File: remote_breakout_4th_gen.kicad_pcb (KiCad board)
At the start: 2 copper layers, 12.5 x 12.1 mm, 3 parts, among them J1 Conn_01x04, J2 Conn_02x04_Odd_Even, J3 Conn_01x04

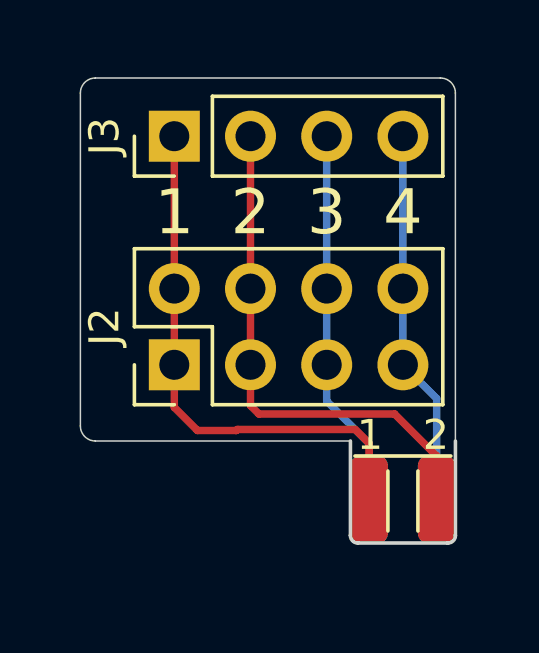
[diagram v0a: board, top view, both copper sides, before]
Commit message: Fill unused areas with copper, update remote connector with connector pads
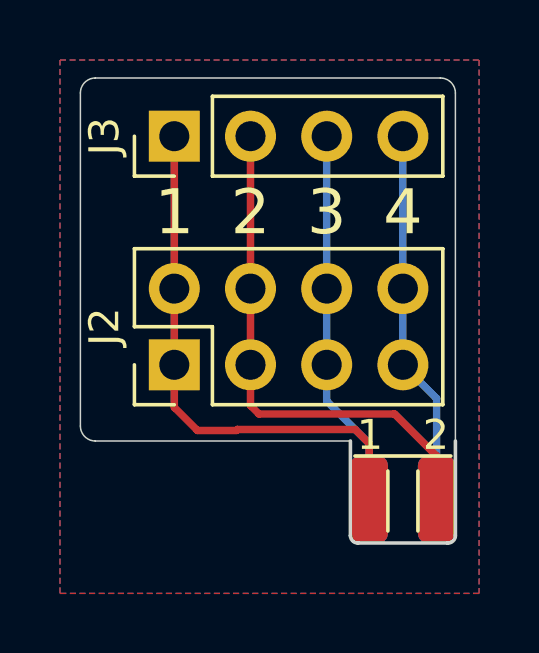
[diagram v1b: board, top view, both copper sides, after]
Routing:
- added copper zone on B.Cu, net (none)
- added copper zone on F.Cu, net (none)
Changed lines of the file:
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@@
       (effects (font (size 1 1) (thickness 0.15)))
     )
+    (fp_text user %R (at 0 3.81) (layer F.Fab)
+      (effects (font (size 1 1) (thickness 0.15)))
+    )
+    (fp_line (start -0.635 -1.27) (end 1.27 -1.27) (layer F.Fab) (width 0.1))
+    (fp_line (start 1.27 -1.27) (end 1.27 8.89) (layer F.Fab) (width 0.1))
+    (fp_line (start 1.27 8.89) (end -1.27 8.89) (layer F.Fab) (width 0.1))
+    (fp_line (start -1.27 8.89) (end -1.27 -0.635) (layer F.Fab) (width 0.1))
+    (fp_line (start -1.27 -0.635) (end -0.635 -1.27) (layer F.Fab) (width 0.1))
+    (fp_line (start -1.33 8.95) (end 1.33 8.95) (layer F.SilkS) (width 0.12))
+    (fp_line (start -1.33 1.27) (end -1.33 8.95) (layer F.SilkS) (width 0.12))
+    (fp_line (start 1.33 1.27) (end 1.33 8.95) (layer F.SilkS) (width 0.12))
+    (fp_line (start -1.33 1.27) (end 1.33 1.27) (layer F.SilkS) (width 0.12))
+    (fp_line (start -1.33 0) (end -1.33 -1.33) (layer F.SilkS) (width 0.12))
+    (fp_line (start -1.33 -1.33) (end 0 -1.33) (layer F.SilkS) (width 0.12))
+    (fp_line (start -1.8 -1.8) (end -1.8 9.4) (layer F.CrtYd) (width 0.05))
+    (fp_line (start -1.8 9.4) (end 1.8 9.4) (layer F.CrtYd) (width 0.05))
+    (fp_line (start 1.8 9.4) (end 1.8 -1.8) (layer F.CrtYd) (width 0.05))
     (fp_line (start 1.8 -1.8) (end -1.8 -1.8) (layer F.CrtYd) (width 0.05))
-    (fp_line (start 1.8 9.4) (end 1.8 -1.8) (layer F.CrtYd) (width 0.05))
-    (fp_line (start -1.8 9.4) (end 1.8 9.4) (layer F.CrtYd) (width 0.05))
-    (fp_line (start -1.8 -1.8) (end -1.8 9.4) (layer F.CrtYd) (width 0.05))
-    (fp_line (start -1.33 -1.33) (end 0 -1.33) (layer F.SilkS) (width 0.12))
-    (fp_line (start -1.33 0) (end -1.33 -1.33) (layer F.SilkS) (width 0.12))
-    (fp_line (start -1.33 1.27) (end 1.33 1.27) (layer F.SilkS) (width 0.12))
-    (fp_line (start 1.33 1.27) (end 1.33 8.95) (layer F.SilkS) (width 0.12))
-    (fp_line (start -1.33 1.27) (end -1.33 8.95) (layer F.SilkS) (width 0.12))
-    (fp_line (start -1.33 8.95) (end 1.33 8.95) (layer F.SilkS) (width 0.12))
-    (fp_line (start -1.27 -0.635) (end -0.635 -1.27) (layer F.Fab) (width 0.1))
-    (fp_line (start -1.27 8.89) (end -1.27 -0.635) (layer F.Fab) (width 0.1))
-    (fp_line (start 1.27 8.89) (end -1.27 8.89) (layer F.Fab) (width 0.1))
-    (fp_line (start 1.27 -1.27) (end 1.27 8.89) (layer F.Fab) (width 0.1))
-    (fp_line (start -0.635 -1.27) (end 1.27 -1.27) (layer F.Fab) (width 0.1))
-    (fp_text user %R (at 0 3.81) (layer F.Fab)
-      (effects (font (size 1 1) (thickness 0.15)))
-    )
     (pad 4 thru_hole oval (at 0 7.62 90) (size 1.7 1.7) (drill 1) (layers *.Cu *.Mask)
       (net 3 /4))
@@
       (effects (font (size 1 1) (thickness 0.15)))
     )
+    (fp_text user %R (at 1.27 3.81) (layer F.Fab)
+      (effects (font (size 1 1) (thickness 0.15)))
+    )
+    (fp_line (start 0 -1.27) (end 3.81 -1.27) (layer F.Fab) (width 0.1))
+    (fp_line (start 3.81 -1.27) (end 3.81 8.89) (layer F.Fab) (width 0.1))
+    (fp_line (start 3.81 8.89) (end -1.27 8.89) (layer F.Fab) (width 0.1))
+    (fp_line (start -1.27 8.89) (end -1.27 0) (layer F.Fab) (width 0.1))
+    (fp_line (start -1.27 0) (end 0 -1.27) (layer F.Fab) (width 0.1))
+    (fp_line (start -1.33 8.95) (end 3.87 8.95) (layer F.SilkS) (width 0.12))
+    (fp_line (start -1.33 1.27) (end -1.33 8.95) (layer F.SilkS) (width 0.12))
+    (fp_line (start 3.87 -1.33) (end 3.87 8.95) (layer F.SilkS) (width 0.12))
+    (fp_line (start -1.33 1.27) (end 1.27 1.27) (layer F.SilkS) (width 0.12))
+    (fp_line (start 1.27 1.27) (end 1.27 -1.33) (layer F.SilkS) (width 0.12))
+    (fp_line (start 1.27 -1.33) (end 3.87 -1.33) (layer F.SilkS) (width 0.12))
+    (fp_line (start -1.33 0) (end -1.33 -1.33) (layer F.SilkS) (width 0.12))
+    (fp_line (start -1.33 -1.33) (end 0 -1.33) (layer F.SilkS) (width 0.12))
+    (fp_line (start -1.8 -1.8) (end -1.8 9.4) (layer F.CrtYd) (width 0.05))
+    (fp_line (start -1.8 9.4) (end 4.35 9.4) (layer F.CrtYd) (width 0.05))
+    (fp_line (start 4.35 9.4) (end 4.35 -1.8) (layer F.CrtYd) (width 0.05))
     (fp_line (start 4.35 -1.8) (end -1.8 -1.8) (layer F.CrtYd) (width 0.05))
-    (fp_line (start 4.35 9.4) (end 4.35 -1.8) (layer F.CrtYd) (width 0.05))
-    (fp_line (start -1.8 9.4) (end 4.35 9.4) (layer F.CrtYd) (width 0.05))
-    (fp_line (start -1.8 -1.8) (end -1.8 9.4) (layer F.CrtYd) (width 0.05))
-    (fp_line (start -1.33 -1.33) (end 0 -1.33) (layer F.SilkS) (width 0.12))
-    (fp_line (start -1.33 0) (end -1.33 -1.33) (layer F.SilkS) (width 0.12))
-    (fp_line (start 1.27 -1.33) (end 3.87 -1.33) (layer F.SilkS) (width 0.12))
-    (fp_line (start 1.27 1.27) (end 1.27 -1.33) (layer F.SilkS) (width 0.12))
-    (fp_line (start -1.33 1.27) (end 1.27 1.27) (layer F.SilkS) (width 0.12))
-    (fp_line (start 3.87 -1.33) (end 3.87 8.95) (layer F.SilkS) (width 0.12))
-    (fp_line (start -1.33 1.27) (end -1.33 8.95) (layer F.SilkS) (width 0.12))
-    (fp_line (start -1.33 8.95) (end 3.87 8.95) (layer F.SilkS) (width 0.12))
-    (fp_line (start -1.27 0) (end 0 -1.27) (layer F.Fab) (width 0.1))
-    (fp_line (start -1.27 8.89) (end -1.27 0) (layer F.Fab) (width 0.1))
-    (fp_line (start 3.81 8.89) (end -1.27 8.89) (layer F.Fab) (width 0.1))
-    (fp_line (start 3.81 -1.27) (end 3.81 8.89) (layer F.Fab) (width 0.1))
-    (fp_line (start 0 -1.27) (end 3.81 -1.27) (layer F.Fab) (width 0.1))
-    (fp_text user %R (at 1.27 3.81) (layer F.Fab)
-      (effects (font (size 1 1) (thickness 0.15)))
-    )
     (pad 8 thru_hole oval (at 2.54 7.62 90) (size 1.7 1.7) (drill 1) (layers *.Cu *.Mask)
       (net 3 /4))
@@
       (effects (font (size 1 1) (thickness 0.15)))
     )
+    (fp_text user 4 (at 1.1 -0.2) (layer B.SilkS)
+      (effects (font (size 1 1) (thickness 0.15)) (justify mirror))
+    )
+    (fp_text user 3 (at -1.1 -0.2) (layer B.SilkS)
+      (effects (font (size 1 1) (thickness 0.15)) (justify mirror))
+    )
+    (fp_text user 2 (at 1.1 -0.2) (layer F.SilkS)
+      (effects (font (size 1 1) (thickness 0.15)))
+    )
+    (fp_text user 1 (at -1.1 -0.2) (layer F.SilkS)
+      (effects (font (size 1 1) (thickness 0.15)))
+    )
+    (fp_arc (start 1.5 3.15) (end 1.75 3.15) (angle 90) (layer Edge.Cuts) (width 0.12))
+    (fp_arc (start -1.5 3.15) (end -1.75 3.15) (angle -90) (layer Edge.Cuts) (width 0.12))
     (fp_line (start 0.5 1) (end 0.5 3) (layer F.SilkS) (width 0.12))
     (fp_line (start -0.5 1) (end -0.5 3) (layer F.SilkS) (width 0.12))
@@
     (fp_line (start 1.75 0) (end 1.75 3.15) (layer Edge.Cuts) (width 0.12))
     (fp_line (start -1.75 0) (end -1.75 3.15) (layer Edge.Cuts) (width 0.12))
-    (fp_text user 4 (at 1.1 -0.2) (layer B.SilkS)
-      (effects (font (size 1 1) (thickness 0.15)) (justify mirror))
-    )
-    (fp_text user 3 (at -1.1 -0.2) (layer B.SilkS)
-      (effects (font (size 1 1) (thickness 0.15)) (justify mirror))
-    )
-    (fp_text user 2 (at 1.1 -0.2) (layer F.SilkS)
-      (effects (font (size 1 1) (thickness 0.15)))
-    )
-    (fp_text user 1 (at -1.1 -0.2) (layer F.SilkS)
-      (effects (font (size 1 1) (thickness 0.15)))
-    )
-    (fp_arc (start 1.5 3.15) (end 1.75 3.15) (angle 90) (layer Edge.Cuts) (width 0.12))
-    (fp_arc (start -1.5 3.15) (end -1.75 3.15) (angle -90) (layer Edge.Cuts) (width 0.12))
-    (pad 2 smd roundrect (at 1.125 1.95) (size 1.25 2.9) (layers F.Cu F.Paste F.Mask) (roundrect_rratio 0.25)
-      (net 1 /2))
-    (pad 1 smd roundrect (at -1.125 1.95) (size 1.25 2.9) (layers F.Cu F.Paste F.Mask) (roundrect_rratio 0.25)
-      (net 2 /1))
-    (pad 4 smd roundrect (at 1.125 1.95) (size 1.25 2.9) (layers B.Cu B.Paste B.Mask) (roundrect_rratio 0.25)
-      (net 3 /4))
-    (pad 3 smd roundrect (at -1.125 1.95) (size 1.25 2.9) (layers B.Cu B.Paste B.Mask) (roundrect_rratio 0.25)
+    (pad 2 connect roundrect (at 1.125 1.95) (size 1.25 2.9) (layers F.Cu F.Mask) (roundrect_rratio 0.25)
+      (net 1 /2))
+    (pad 1 connect roundrect (at -1.125 1.95) (size 1.25 2.9) (layers F.Cu F.Mask) (roundrect_rratio 0.25)
+      (net 2 /1))
+    (pad 4 connect roundrect (at 1.125 1.95) (size 1.25 2.9) (layers B.Cu B.Mask) (roundrect_rratio 0.25)
+      (net 3 /4))
+    (pad 3 connect roundrect (at -1.125 1.95) (size 1.25 2.9) (layers B.Cu B.Mask) (roundrect_rratio 0.25)
       (net 4 /3))
   )
@@
   (segment (start -2.54 -2.54) (end -2.54 -5.08) (width 0.25) (layer B.Cu) (net 4))
   (segment (start -2.54 -5.08) (end -2.54 -10.16) (width 0.25) (layer B.Cu) (net 4))
+  (zone (net 0) (net_name "") (layer F.Cu) (hatch edge 0.508)
+    (connect_pads (clearance 0.508))
+    (min_thickness 0.254)
+    (fill yes (arc_segments 32) (thermal_gap 0.508) (thermal_bridge_width 0.508))
+    (polygon
+      (pts
+        (xy 2.54 5.08) (xy -11.43 5.08) (xy -11.43 -12.7) (xy 2.54 -12.7)
+      )
+    )
+  )
+  (zone (net 0) (net_name "") (layer B.Cu) (hatch edge 0.508)
+    (connect_pads (clearance 0.508))
+    (min_thickness 0.254)
+    (fill yes (arc_segments 32) (thermal_gap 0.508) (thermal_bridge_width 0.508))
+    (polygon
+      (pts
+        (xy 2.54 5.08) (xy -11.43 5.08) (xy -11.43 -12.7) (xy 2.54 -12.7)
+      )
+    )
+  )
 )

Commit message: Prepare for JLCPCB
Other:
- board text added: "JLCJLCJLCJLC"
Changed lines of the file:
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@@
   (general
     (thickness 1.6)
-    (drawings 16)
+    (drawings 17)
     (tracks 25)
     (zones 0)
@@
     (visible_elements 7FFFFFFF)
     (pcbplotparams
-      (layerselection 0x00030_7ffffffe)
+      (layerselection 0x010fc_ffffffff)
       (usegerberextensions false)
       (usegerberattributes true)
@@
       (padsonsilk false)
       (subtractmaskfromsilk false)
-      (outputformat 3)
+      (outputformat 1)
       (mirror false)
       (drillshape 0)
       (scaleselection 1)
-      (outputdirectory ""))
+      (outputdirectory "export_remote/"))
   )
   (net 0 "")
@@
       (effects (font (size 1 1) (thickness 0.15)))
     )
-    (fp_text user %R (at 0 3.81) (layer F.Fab)
-      (effects (font (size 1 1) (thickness 0.15)))
-    )
     (fp_line (start -0.635 -1.27) (end 1.27 -1.27) (layer F.Fab) (width 0.1))
     (fp_line (start 1.27 -1.27) (end 1.27 8.89) (layer F.Fab) (width 0.1))
@@
     (fp_line (start 1.8 9.4) (end 1.8 -1.8) (layer F.CrtYd) (width 0.05))
     (fp_line (start 1.8 -1.8) (end -1.8 -1.8) (layer F.CrtYd) (width 0.05))
+    (fp_text user %R (at 0 3.81) (layer F.Fab)
+      (effects (font (size 1 1) (thickness 0.15)))
+    )
     (pad 4 thru_hole oval (at 0 7.62 90) (size 1.7 1.7) (drill 1) (layers *.Cu *.Mask)
       (net 3 /4))
@@
     )
     (fp_text value Conn_02x04_Odd_Even (at -3.81 -3.78 180) (layer F.Fab)
-      (effects (font (size 1 1) (thickness 0.15)))
-    )
-    (fp_text user %R (at 1.27 3.81) (layer F.Fab)
       (effects (font (size 1 1) (thickness 0.15)))
     )
@@
     (fp_line (start 4.35 9.4) (end 4.35 -1.8) (layer F.CrtYd) (width 0.05))
     (fp_line (start 4.35 -1.8) (end -1.8 -1.8) (layer F.CrtYd) (width 0.05))
+    (fp_text user %R (at 1.27 3.81) (layer F.Fab)
+      (effects (font (size 1 1) (thickness 0.15)))
+    )
     (pad 8 thru_hole oval (at 2.54 7.62 90) (size 1.7 1.7) (drill 1) (layers *.Cu *.Mask)
       (net 3 /4))
@@
       (effects (font (size 1 1) (thickness 0.15)))
     )
-    (fp_text user 4 (at 1.1 -0.2) (layer B.SilkS)
-      (effects (font (size 1 1) (thickness 0.15)) (justify mirror))
-    )
-    (fp_text user 3 (at -1.1 -0.2) (layer B.SilkS)
-      (effects (font (size 1 1) (thickness 0.15)) (justify mirror))
-    )
-    (fp_text user 2 (at 1.1 -0.2) (layer F.SilkS)
-      (effects (font (size 1 1) (thickness 0.15)))
-    )
-    (fp_text user 1 (at -1.1 -0.2) (layer F.SilkS)
-      (effects (font (size 1 1) (thickness 0.15)))
-    )
-    (fp_arc (start 1.5 3.15) (end 1.75 3.15) (angle 90) (layer Edge.Cuts) (width 0.12))
-    (fp_arc (start -1.5 3.15) (end -1.75 3.15) (angle -90) (layer Edge.Cuts) (width 0.12))
     (fp_line (start 0.5 1) (end 0.5 3) (layer F.SilkS) (width 0.12))
     (fp_line (start -0.5 1) (end -0.5 3) (layer F.SilkS) (width 0.12))
@@
     (fp_line (start 1.75 0) (end 1.75 3.15) (layer Edge.Cuts) (width 0.12))
     (fp_line (start -1.75 0) (end -1.75 3.15) (layer Edge.Cuts) (width 0.12))
+    (fp_text user 4 (at 1.1 -0.2) (layer B.SilkS)
+      (effects (font (size 1 1) (thickness 0.15)) (justify mirror))
+    )
+    (fp_text user 3 (at -1.1 -0.2) (layer B.SilkS)
+      (effects (font (size 1 1) (thickness 0.15)) (justify mirror))
+    )
+    (fp_text user 2 (at 1.1 -0.2) (layer F.SilkS)
+      (effects (font (size 1 1) (thickness 0.15)))
+    )
+    (fp_text user 1 (at -1.1 -0.2) (layer F.SilkS)
+      (effects (font (size 1 1) (thickness 0.15)))
+    )
+    (fp_arc (start 1.5 3.15) (end 1.75 3.15) (angle 90) (layer Edge.Cuts) (width 0.12))
+    (fp_arc (start -1.5 3.15) (end -1.75 3.15) (angle -90) (layer Edge.Cuts) (width 0.12))
     (pad 2 connect roundrect (at 1.125 1.95) (size 1.25 2.9) (layers F.Cu F.Mask) (roundrect_rratio 0.25)
       (net 1 /2))
@@
       (net 4 /3))
   )
+  (gr_text JLCJLCJLCJLC (at -9.525 -6.35 90) (layer B.SilkS)
+    (effects (font (size 0.8 0.8) (thickness 0.15)) (justify mirror))
+  )
   (gr_text "Receptacle is approx 1.9 mm at the widest,\nUse 1.6 mm board for best fit" (at -5 -15) (layer Cmts.User)
